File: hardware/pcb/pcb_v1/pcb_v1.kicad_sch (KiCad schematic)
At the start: 21 parts, among them J1 Conn_01x10, J2 Conn_01x10, J3 Conn_01x10, J4 Conn_01x10, U1 Pico

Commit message: pcbv1 updated (MC34166 added)
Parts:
- added D17: 1N5822, Diode_THT:D_DO-201AD_P15.24mm_Horizontal, symbol Diode:1N5822
- added U2: MC34166, Package_TO_SOT_SMD:TO-263-5_TabPin3, symbol MC34166:MC34166
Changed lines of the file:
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@@
     (stroke (width 0) (type default) (color 0 0 0 0))
+  )
+  (symbol (lib_id "MC34166:MC34166") (at 91.44 44.45 0) (unit 1)
+    (in_bom yes) (on_board yes)
+    (property "Reference" "U2" (id 0) (at 92.075 31.75 0))
+    (property "Value" "MC34166" (id 1) (at 92.075 34.29 0))
+    (property "Footprint" "Package_TO_SOT_SMD:TO-263-5_TabPin3" (id 2) (at 91.44 57.15 0)
+      (effects (font (size 1.27 1.27)) hide)
+    )
+    (property "Datasheet" "" (id 3) (at 91.44 44.45 0)
+      (effects (font (size 1.27 1.27)) hide)
+    )
+    (pin "1")
+    (pin "2")
+    (pin "3")
+    (pin "4")
+    (pin "5")
   )
   (symbol (lib_id "power:+5V") (at 170.18 40.64 0) (unit 1)
@@
     (pin "4")
   )
+  (symbol (lib_id "Diode:1N5822") (at 82.55 62.23 0) (unit 1)
+    (in_bom yes) (on_board yes) (fields_autoplaced)
+    (property "Reference" "D17" (id 0) (at 82.2325 55.88 0))
+    (property "Value" "1N5822" (id 1) (at 82.2325 58.42 0))
+    (property "Footprint" "Diode_THT:D_DO-201AD_P15.24mm_Horizontal" (id 2) (at 82.55 66.675 0)
+      (effects (font (size 1.27 1.27)) hide)
+    )
+    (property "Datasheet" "http://www.vishay.com/docs/88526/1n5820.pdf" (id 3) (at 82.55 62.23 0)
+      (effects (font (size 1.27 1.27)) hide)
+    )
+    (pin "1")
+    (pin "2")
+  )
   (symbol (lib_id "Connector_Generic:Conn_01x10") (at 39.37 152.4 0) (mirror y) (unit 1)
     (in_bom yes) (on_board yes) (fields_autoplaced)
@@
       (reference "D16") (unit 1) (value "WS2812B") (footprint "LED_SMD:LED_WS2812B_PLCC4_5.0x5.0mm_P3.2mm")
     )
+    (path "/f5a97da1-282d-43a4-ae5f-607cebde55a6"
+      (reference "D17") (unit 1) (value "1N5822") (footprint "Diode_THT:D_DO-201AD_P15.24mm_Horizontal")
+    )
     (path "/2a3f5b67-1280-4816-b0e5-adea4657ddfb"
       (reference "J1") (unit 1) (value "Conn_01x10") (footprint "Connector_PinHeader_2.54mm:PinHeader_2x05_P2.54mm_Vertical")
@@
       (reference "U1") (unit 1) (value "Pico") (footprint "MCU_RaspberryPi_and_Boards:RPi_Pico_SMD_TH")
     )
-  )
+    (path "/054e6c56-d839-4274-ab30-933acc22d5ba"
+      (reference "U2") (unit 1) (value "MC34166") (footprint "Package_TO_SOT_SMD:TO-263-5_TabPin3")
+    )
+  )

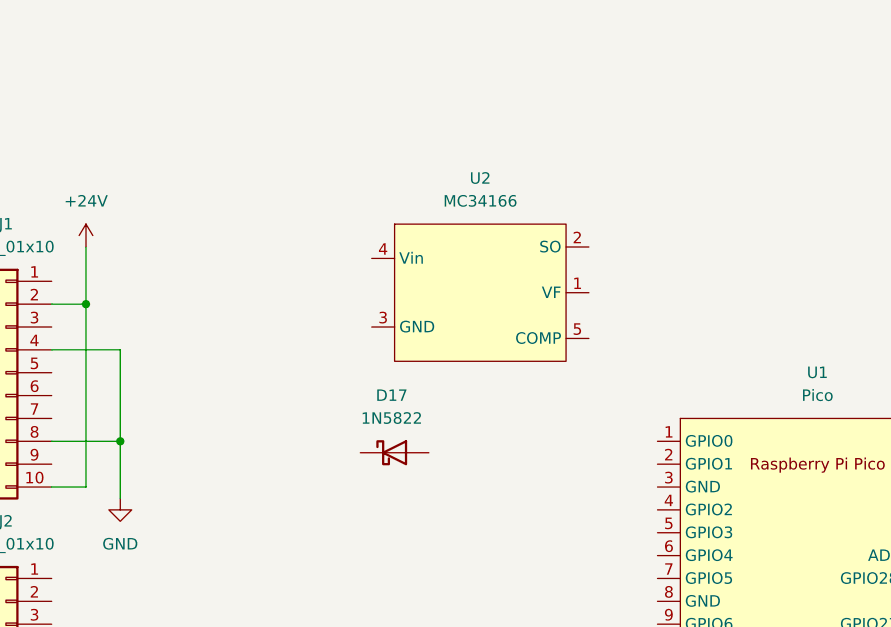
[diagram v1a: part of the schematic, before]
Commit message: TL2575-05 added
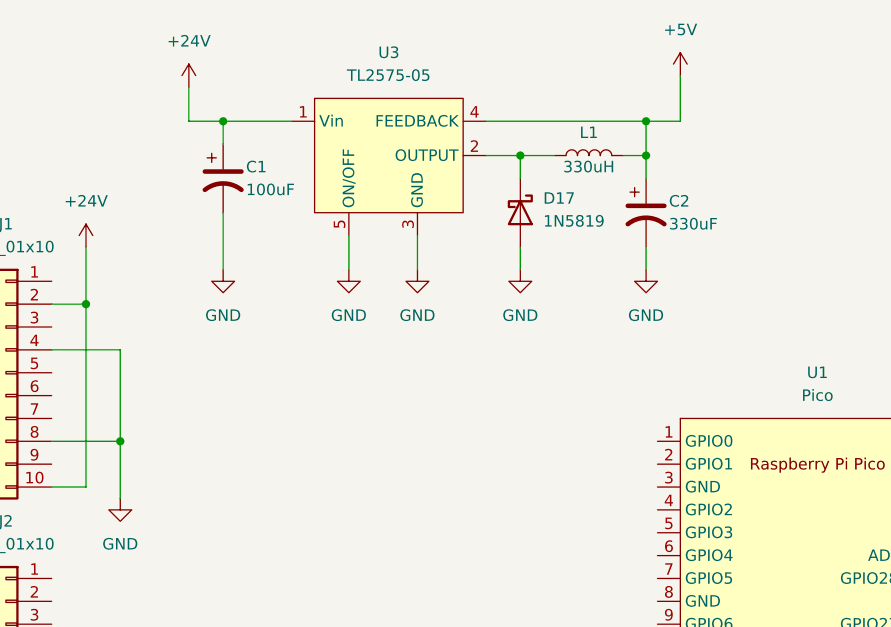
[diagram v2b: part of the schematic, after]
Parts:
- removed D17: 1N5822, Diode_THT:D_DO-201AD_P15.24mm_Horizontal, symbol Diode:1N5822
- removed U2: MC34166, Package_TO_SOT_SMD:TO-263-5_TabPin3, symbol MC34166:MC34166
- added C1: 100uF, symbol Device:C_Polarized_US
- added C2: 330uF, symbol Device:C_Polarized_US
- added D17: 1N5819, Diode_THT:D_DO-41_SOD81_P10.16mm_Horizontal, symbol Diode:1N5819
- added L1: 330uH, symbol Device:L
- added U3: TL2575-05, symbol TL2575-05:TL2575-05
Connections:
- net +24V: now also C1.1, U3.1 (Vin)
- net +5V: now also C2.1, L1.2, U3.4 (FEEDBACK)
- net GND: now also C1.2, C2.2, D17.2 (A), U3.3 (GND), U3.5 (ON/OFF)
- new net: D17.1 (K), L1.1, U3.2 (OUTPUT)

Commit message: worked on pcbv1
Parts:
- added C1, C10, C11, C12, C13, C14, C15, C16, C2, C3, C4, C5, C6, C7, C8, C9: 100nF, Capacitor_SMD:C_0805_2012Metric, symbol Device:C
- C17: renamed from C1; footprint (none) -> Capacitor_SMD:CP_Elec_8x10
- C18: renamed from C2; footprint (none) -> Capacitor_SMD:CP_Elec_10x10
- L1: footprint (none) -> Inductor_SMD:L_12x12mm_H8mm
- U2: renamed from U3; footprint (none) -> Package_TO_SOT_SMD:TO-263-5_TabPin3
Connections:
- net +24V: now also J2.10 (Pin_10), J2.2 (Pin_2), J3.10 (Pin_10), J3.2 (Pin_2), J4.10 (Pin_10), J4.2 (Pin_2)
- net +5V: now also U1.39 (VSYS), C1.2, C10.2, C11.2, C12.2, C13.2, C14.2, C15.2, C16.2, C2.2, C3.2, C4.2, C5.2, C6.2, C7.2, C8.2, C9.2
- net GND: now also J2.4 (Pin_4), J2.8 (Pin_8), J3.4 (Pin_4), J3.8 (Pin_8), J4.4 (Pin_4), J4.8 (Pin_8), U1.13 (GND), U1.18 (GND), U1.23 (GND), U1.28 (GND), U1.3 (GND), U1.33 (AGND), U1.38 (GND), U1.8 (GND), C1.1, C10.1, C11.1, C12.1, C13.1, C14.1, C15.1, C16.1, C2.1, C3.1, C4.1, C5.1, C6.1, C7.1, C8.1, C9.1
- net at D16.2 (DOUT): no longer U1.26 (GPIO20)
- net at U1.27 (GPIO21): no longer D1.4 (DIN)
- net RGB_IN: now reaches U1.6 (GPIO4)
- net RGB_IN: now also D1.4 (DIN)
- no-connect marks 0 -> 1
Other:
- note added: "CONNECTOREN"
- note added: "PICO"
- note added: "RGB LEDS"
- note added: "VOEDING"
- moved on the sheet: C17, C18, D1, D10, D11, D12, D13, D14, D15, D16, D17, D2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

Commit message: finished pcbv1
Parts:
- added J5, J6: Conn_01x10, Connector_PinHeader_2.54mm:PinHeader_2x05_P2.54mm_Vertical, symbol Connector_Generic:Conn_01x10
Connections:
- net +24V: now also J1.3 (Pin_3), J1.7 (Pin_7), J2.3 (Pin_3), J2.7 (Pin_7), J3.3 (Pin_3), J3.7 (Pin_7), J4.3 (Pin_3), J4.7 (Pin_7), J5.3 (Pin_3), J5.7 (Pin_7), J6.3 (Pin_3), J6.7 (Pin_7); no longer J1.10 (Pin_10), J1.2 (Pin_2), J2.10 (Pin_10), J2.2 (Pin_2), J3.10 (Pin_10), J3.2 (Pin_2), J4.10 (Pin_10), J4.2 (Pin_2)
- net GND: now also J5.4 (Pin_4), J5.8 (Pin_8), J6.4 (Pin_4), J6.8 (Pin_8)
- net SDA: now reaches J1.1 (Pin_1)
- net SDA: now also J1.9 (Pin_9), J2.1 (Pin_1), J2.9 (Pin_9), J3.1 (Pin_1), J3.9 (Pin_9), J4.1 (Pin_1), J4.9 (Pin_9), U1.31 (GPIO26_ADC0), J5.1 (Pin_1), J5.9 (Pin_9), J6.1 (Pin_1), J6.9 (Pin_9)
- net SEL1: now reaches J1.5 (Pin_5)
- net SEL1: now also J1.6 (Pin_6), U1.4 (GPIO2)
- net SEL3: now reaches U1.1 (GPIO0)
- net SEL3: now also J3.5 (Pin_5), J3.6 (Pin_6)
- net SEL2: now reaches U1.2 (GPIO1)
- net SEL2: now also J2.5 (Pin_5), J2.6 (Pin_6)
- net SEL6: now reaches U1.20 (GPIO15)
- net SEL6: now also J6.5 (Pin_5), J6.6 (Pin_6)
- net SEL5: now reaches U1.21 (GPIO16)
- net SEL5: now also J5.5 (Pin_5), J5.6 (Pin_6)
- net SEL4: now reaches U1.22 (GPIO17)
- net SEL4: now also J4.5 (Pin_5), J4.6 (Pin_6)
- net SCL: now reaches U1.32 (GPIO27_ADC1)
- net SCL: now also J1.10 (Pin_10), J1.2 (Pin_2), J2.10 (Pin_10), J2.2 (Pin_2), J3.10 (Pin_10), J3.2 (Pin_2), J4.10 (Pin_10), J4.2 (Pin_2), J5.10 (Pin_10), J5.2 (Pin_2), J6.10 (Pin_10), J6.2 (Pin_2)
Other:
- title: (none) -> Lannooleaf PCB schema
- moved on the sheet: C1, C10, C11, C12, C13, C14, C15, C16, C2, C3, C4, C5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

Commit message: worked on pcbv1
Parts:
- removed D17: 1N5819, Diode_THT:D_DO-41_SOD81_P10.16mm_Horizontal, symbol Diode:1N5819
- removed U2: TL2575-05, Package_TO_SOT_SMD:TO-263-5_TabPin3, symbol TL2575-05:TL2575-05
- added D17: 1N5822, Diode_THT:D_DO-201AD_P15.24mm_Horizontal, symbol Diode:1N5822
- added J7: Barrel_Jack_Switch, Connector_BarrelJack:BarrelJack_CLIFF_FC681465S_SMT_Horizontal, symbol Connector:Barrel_Jack_Switch
- added J8: Conn_01x05, Connector_PinSocket_2.54mm:PinSocket_1x05_P2.54mm_Horizontal, symbol Connector_Generic:Conn_01x05
- added J9: Barrel_Jack_Switch, symbol Connector:Barrel_Jack_Switch
- added R1: 3.1k, Resistor_SMD:R_0805_2012Metric, symbol Device:R
- added R2: 1k, Resistor_SMD:R_0805_2012Metric, symbol Device:R
- added U2: LM2596S-ADJ, Package_TO_SOT_SMD:TO-263-5_TabPin3, symbol Regulator_Switching:LM2596S-ADJ
- C18: value 330uF -> 220uF
- L1: value 330uH -> 33uH
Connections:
- net +24V: now also J1.10 (Pin_10), J1.2 (Pin_2), J2.10 (Pin_10), J2.2 (Pin_2), J3.10 (Pin_10), J3.2 (Pin_2), J4.10 (Pin_10), J4.2 (Pin_2), J5.10 (Pin_10), J5.2 (Pin_2), J6.10 (Pin_10), J6.2 (Pin_2), J7.1, U2.1 (VIN); no longer J1.3 (Pin_3), J1.7 (Pin_7), J2.3 (Pin_3), J2.7 (Pin_7), J3.3 (Pin_3), J3.7 (Pin_7), J4.3 (Pin_3), J4.7 (Pin_7), J5.3 (Pin_3), J5.7 (Pin_7), J6.3 (Pin_3), J6.7 (Pin_7)
- net +5V: now also R1.2
- net GND: now also J1.1 (Pin_1), J1.9 (Pin_9), J2.1 (Pin_1), J2.9 (Pin_9), J3.1 (Pin_1), J3.9 (Pin_9), J4.1 (Pin_1), J4.9 (Pin_9), J5.1 (Pin_1), J5.9 (Pin_9), J6.1 (Pin_1), J6.9 (Pin_9), D17.2 (A), J7.2, J7.3, J8.3 (Pin_3), R2.1, U2.3 (GND), U2.5 (~{ON}/OFF); no longer J1.4 (Pin_4), J1.8 (Pin_8), J2.4 (Pin_4), J2.8 (Pin_8), J3.4 (Pin_4), J3.8 (Pin_8), J4.4 (Pin_4), J4.8 (Pin_8), J5.4 (Pin_4), J5.8 (Pin_8), J6.4 (Pin_4), J6.8 (Pin_8)
- net SCL: now also J1.4 (Pin_4), J1.8 (Pin_8), J2.4 (Pin_4), J2.8 (Pin_8), J3.4 (Pin_4), J3.8 (Pin_8), J4.4 (Pin_4), J4.8 (Pin_8), J5.4 (Pin_4), J5.8 (Pin_8), J6.4 (Pin_4), J6.8 (Pin_8), U1.12 (GPIO9); no longer J1.10 (Pin_10), J1.2 (Pin_2), J2.10 (Pin_10), J2.2 (Pin_2), J3.10 (Pin_10), J3.2 (Pin_2), J4.10 (Pin_10), J4.2 (Pin_2), J5.10 (Pin_10), J5.2 (Pin_2), J6.10 (Pin_10), J6.2 (Pin_2), U1.32 (GPIO27_ADC1)
- net SDA: now also J1.3 (Pin_3), J1.7 (Pin_7), J2.3 (Pin_3), J2.7 (Pin_7), J3.3 (Pin_3), J3.7 (Pin_7), J4.3 (Pin_3), J4.7 (Pin_7), J5.3 (Pin_3), J5.7 (Pin_7), J6.3 (Pin_3), J6.7 (Pin_7), U1.11 (GPIO8); no longer J1.1 (Pin_1), J1.9 (Pin_9), J2.1 (Pin_1), J2.9 (Pin_9), J3.1 (Pin_1), J3.9 (Pin_9), J4.1 (Pin_1), J4.9 (Pin_9), J5.1 (Pin_1), J5.9 (Pin_9), J6.1 (Pin_1), J6.9 (Pin_9), U1.31 (GPIO26_ADC0)
- net SEL1: now also U1.9 (GPIO6); no longer U1.4 (GPIO2)
- net SEL2: now also U1.7 (GPIO5); no longer U1.2 (GPIO1)
- net SEL3: now also U1.34 (GPIO28_ADC2); no longer U1.1 (GPIO0)
- net SEL4: now also U1.24 (GPIO18); no longer U1.22 (GPIO17)
- net at L1.1: now also D17.1 (K), U2.2 (OUT)
- net TX: now reaches U1.5 (GPIO3)
- net TX: now also J8.5 (Pin_5)
- new net: R1.1, R2.2, U2.4 (FB)
- new net CS: J8.2 (Pin_2), U1.2 (GPIO1)
- new net CSK: J8.4 (Pin_4), U1.4 (GPIO2)
- new net RX: J8.1 (Pin_1), U1.1 (GPIO0)
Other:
- note added: "POWER CONNECTOR"
- note added: "SPI CONNECTOR"
- moved on the sheet: C1, C10, C11, C12, C13, C14, C15, C16, C17, C18, C2, C3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

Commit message: worked on pcbv1
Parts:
- removed J9: Barrel_Jack_Switch, symbol Connector:Barrel_Jack_Switch
- C17: footprint Capacitor_SMD:CP_Elec_8x10 -> Capacitor_SMD:CP_Elec_10x10
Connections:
- no-connect marks 1 -> 22
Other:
- moved on the sheet: C1, C10, C11, C12, C13, C14, C15, C16, C2, C3, C4, C5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

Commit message: pcb updated
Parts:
- removed D17: 1N5822, Diode_THT:D_DO-201AD_P15.24mm_Horizontal, symbol Diode:1N5822
- added C17, C22: 1nF, Capacitor_SMD:C_0805_2012Metric, symbol Device:C
- added C18, C23: 100nF, Capacitor_SMD:C_0805_2012Metric, symbol Device:C
- added C19, C24: 1uF, Capacitor_SMD:C_0805_2012Metric, symbol Device:C
- added D17: SS34, Diode_SMD:D_SMC_Handsoldering, symbol Device:D_Schottky
- C20: renamed from C17; footprint Capacitor_SMD:CP_Elec_10x10 -> Capacitor_SMD:CP_Elec_10x10.5
- C21: renamed from C18; footprint Capacitor_SMD:CP_Elec_10x10 -> Capacitor_SMD:CP_Elec_10x10.5
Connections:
- net +24V: now also C17.1, C18.1, C19.1
- net +5V: now also C22.1, C23.1, C24.1
- net GND: now also C17.2, C18.2, C19.2, C22.2, C23.2, C24.2, D17.2 (A)
- net at L1.1, U2.2 (OUT): now also D17.1 (K)
- no-connect marks 22 -> 23
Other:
- moved on the sheet: C1, C10, C11, C12, C13, C14, C15, C16, C2, C20, C21, C3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

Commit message: modified pcb
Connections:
- no-connect marks 23 -> 22
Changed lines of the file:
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@@
   (junction (at 107.95 102.87) (diameter 0) (color 0 0 0 0)
   )
-  (no_connect (at 199.39 177.8))
   (no_connect (at 269.24 133.35))
   (no_connect (at 140.97 39.37))
